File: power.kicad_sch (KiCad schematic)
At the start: 8 parts, among them U8 LM2940S-5.0/NOPB

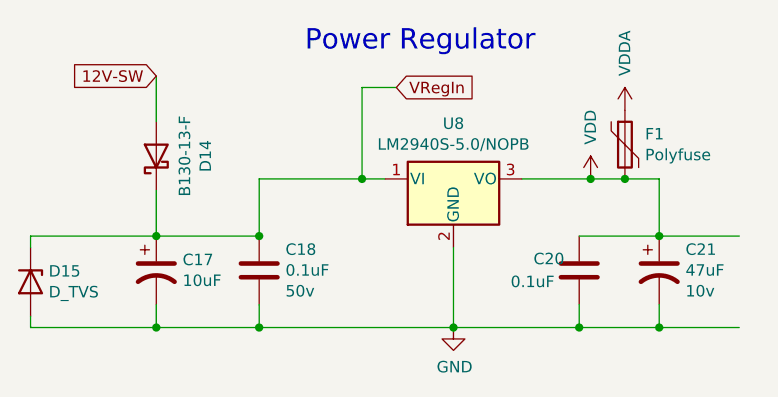
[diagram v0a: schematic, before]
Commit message: Boards should be placed correctly now
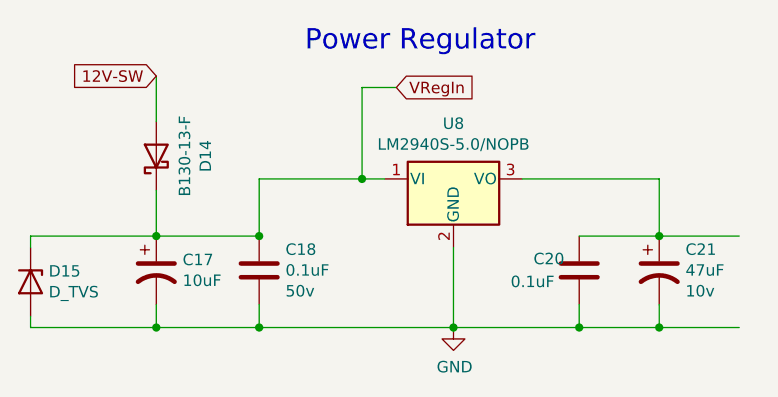
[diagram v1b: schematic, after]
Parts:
- removed F1: Polyfuse, Fuse:Fuse_1812_4532Metric, symbol Device:Polyfuse
- C17: JLCPCB (none) -> C122299
- C18, C20: JLCPCB (none) -> C49678
- C21: JLCPCB (none) -> C7207
- D14: JLCPCB (none) -> C134423
- D15: JLCPCB (none) -> C294881
- U8: footprint Package_TO_SOT_SMD:TO-263-3_TabPin2 -> Package_TO_SOT_SMD:SOT-223; JLCPCB (none) -> C596334
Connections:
- net VDD: no longer names the net of C20.1, C21.1, U8.3 (VO)
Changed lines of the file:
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@@
     (company "Speeduino")
   )
-  (junction (at 176.53 62.23) (diameter 0) (color 0 0 0 0)
-  )
   (junction (at 128.27 78.74) (diameter 0) (color 0 0 0 0)
   )
@@
   (junction (at 128.27 68.58) (diameter 0) (color 0 0 0 0)
   )
-  (junction (at 180.34 62.23) (diameter 0) (color 0 0 0 0)
-  )
   (junction (at 139.7 78.74) (diameter 0) (color 0 0 0 0)
   )
@@
     (stroke (width 0) (type default) (color 0 0 0 0))
   )
-  (wire (pts (xy 168.91 62.23) (xy 176.53 62.23))
+  (wire (pts (xy 168.91 62.23) (xy 184.15 62.23))
     (stroke (width 0) (type default) (color 0 0 0 0))
   )
@@
     (stroke (width 0) (type default) (color 0 0 0 0))
   )
-  (wire (pts (xy 180.34 62.23) (xy 184.15 62.23))
-    (stroke (width 0) (type default) (color 0 0 0 0))
-  )
   (wire (pts (xy 114.3 78.74) (xy 128.27 78.74))
     (stroke (width 0) (type default) (color 0 0 0 0))
   )
   (wire (pts (xy 175.26 76.2) (xy 175.26 78.74))
-    (stroke (width 0) (type default) (color 0 0 0 0))
-  )
-  (wire (pts (xy 176.53 62.23) (xy 180.34 62.23))
     (stroke (width 0) (type default) (color 0 0 0 0))
   )
@@
       (effects (font (size 1.27 1.27)) hide)
     )
+    (property "JLCPCB" "C49678" (id 9) (at 139.7 72.39 0)
+      (effects (font (size 1.27 1.27)) hide)
+    )
     (pin "1")
     (pin "2")
@@
     )
     (property "URL" "https://www.digikey.com/product-detail/en/kemet/T491D106K050AT/399-8361-1-ND/3472084" (id 8) (at 0 144.78 0)
+      (effects (font (size 1.27 1.27)) hide)
+    )
+    (property "JLCPCB" "C122299" (id 9) (at 128.27 72.39 0)
       (effects (font (size 1.27 1.27)) hide)
     )
@@
       (effects (font (size 1.27 1.27)) hide)
     )
-    (pin "1")
-    (pin "2")
-  )
-  (symbol (lib_id "power:VDD") (at 176.53 62.23 0) (unit 1)
-    (in_bom yes) (on_board yes)
-    (property "Reference" "#PWR047" (id 0) (at 176.53 66.04 0)
-      (effects (font (size 1.27 1.27)) hide)
-    )
-    (property "Value" "VDD" (id 1) (at 176.53 58.42 90)
-      (effects (font (size 1.27 1.27)) (justify left))
-    )
-    (property "Footprint" "" (id 2) (at 176.53 62.23 0)
-      (effects (font (size 1.27 1.27)) hide)
-    )
-    (property "Datasheet" "" (id 3) (at 176.53 62.23 0)
-      (effects (font (size 1.27 1.27)) hide)
-    )
-    (pin "1")
+    (property "JLCPCB" "C134423" (id 8) (at 128.27 59.69 0)
+      (effects (font (size 1.27 1.27)) hide)
+    )
+    (pin "1")
+    (pin "2")
   )
   (symbol (lib_id "Device:C") (at 175.26 72.39 0) (unit 1)
@@
       (effects (font (size 1.27 1.27)) hide)
     )
+    (property "JLCPCB" "C49678" (id 8) (at 175.26 72.39 0)
+      (effects (font (size 1.27 1.27)) hide)
+    )
     (pin "1")
     (pin "2")
@@
     )
     (property "URL" "https://www.digikey.com/product-detail/en/avx-corporation/TAJB476K006RNJ/478-1692-1-ND/564724" (id 8) (at 0 144.78 0)
+      (effects (font (size 1.27 1.27)) hide)
+    )
+    (property "JLCPCB" "C7207" (id 9) (at 184.15 72.39 0)
       (effects (font (size 1.27 1.27)) hide)
     )
@@
     (property "Reference" "U8" (id 0) (at 161.29 56.0832 0))
     (property "Value" "LM2940S-5.0/NOPB" (id 1) (at 161.29 58.3946 0))
-    (property "Footprint" "Package_TO_SOT_SMD:TO-263-3_TabPin2" (id 2) (at 161.29 56.515 0)
+    (property "Footprint" "Package_TO_SOT_SMD:SOT-223" (id 2) (at 161.29 56.515 0)
       (effects (font (size 1.27 1.27) italic) hide)
     )
@@
       (effects (font (size 1.27 1.27)) hide)
     )
+    (property "JLCPCB" "C596334" (id 10) (at 161.29 62.23 0)
+      (effects (font (size 1.27 1.27)) hide)
+    )
     (pin "1")
     (pin "2")
     (pin "3")
   )
-  (symbol (lib_id "power:VDDA") (at 180.34 54.61 0) (unit 1)
-    (in_bom yes) (on_board yes)
-    (property "Reference" "#PWR0108" (id 0) (at 180.34 58.42 0)
-      (effects (font (size 1.27 1.27)) hide)
-    )
-    (property "Value" "VDDA" (id 1) (at 180.34 50.8 90)
-      (effects (font (size 1.27 1.27)) (justify left))
-    )
-    (property "Footprint" "" (id 2) (at 180.34 54.61 0)
-      (effects (font (size 1.27 1.27)) hide)
-    )
-    (property "Datasheet" "" (id 3) (at 180.34 54.61 0)
-      (effects (font (size 1.27 1.27)) hide)
-    )
-    (pin "1")
-  )
-  (symbol (lib_id "Device:Polyfuse") (at 180.34 58.42 0) (unit 1)
-    (in_bom yes) (on_board yes)
-    (property "Reference" "F1" (id 0) (at 182.5752 57.2516 0)
-      (effects (font (size 1.27 1.27)) (justify left))
-    )
-    (property "Value" "Polyfuse" (id 1) (at 182.5752 59.563 0)
-      (effects (font (size 1.27 1.27)) (justify left))
-    )
-    (property "Footprint" "Fuse:Fuse_1812_4532Metric" (id 2) (at 181.61 63.5 0)
-      (effects (font (size 1.27 1.27)) (justify left) hide)
-    )
-    (property "Datasheet" "~" (id 3) (at 180.34 58.42 0)
-      (effects (font (size 1.27 1.27)) hide)
-    )
-    (property "Digikey Part Number" "507-1361-1-ND" (id 4) (at 0 116.84 0)
-      (effects (font (size 1.27 1.27)) hide)
-    )
-    (property "Manufacturer_Name" "Bel Fuse" (id 5) (at 0 116.84 0)
-      (effects (font (size 1.27 1.27)) hide)
-    )
-    (property "Manufacturer_Part_Number" "0ZCC0050FF2C" (id 6) (at 0 116.84 0)
-      (effects (font (size 1.27 1.27)) hide)
-    )
-    (property "URL" "https://www.digikey.com.au/product-detail/en/bel-fuse-inc/0ZCC0050FF2C/507-1361-1-ND/1560228" (id 7) (at 0 116.84 0)
-      (effects (font (size 1.27 1.27)) hide)
-    )
-    (pin "1")
-    (pin "2")
-  )
   (symbol (lib_id "Device:D_Zener") (at 114.3 73.66 270) (unit 1)
     (in_bom yes) (on_board yes)
@@
       (effects (font (size 1.27 1.27)) hide)
     )
+    (property "JLCPCB" "C294881" (id 7) (at 114.3 73.66 90)
+      (effects (font (size 1.27 1.27)) hide)
+    )

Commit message: More changes
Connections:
- net +5V: now reaches C20.1, C21.1, U8.3 (VO)
- net 12V-SW renamed +30
- net VRegIn: no longer names the net of C17.1, C18.1, D14.1 (K), D15.1 (K), U8.1 (VI)
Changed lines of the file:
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@@
   (junction (at 184.15 68.58) (diameter 0) (color 0 0 0 0)
   )
-  (junction (at 184.15 78.74) (diameter 0) (color 0 0 0 0)
-  )
-  (junction (at 151.13 62.23) (diameter 0) (color 0 0 0 0)
-  )
   (junction (at 161.29 78.74) (diameter 0) (color 0 0 0 0)
   )
@@
     (stroke (width 0) (type default) (color 0 0 0 0))
   )
-  (wire (pts (xy 154.94 52.07) (xy 151.13 52.07))
-    (stroke (width 0) (type default) (color 0 0 0 0))
-  )
   (wire (pts (xy 114.3 78.74) (xy 114.3 77.47))
     (stroke (width 0) (type default) (color 0 0 0 0))
@@
     (stroke (width 0) (type default) (color 0 0 0 0))
   )
-  (wire (pts (xy 151.13 52.07) (xy 151.13 62.23))
-    (stroke (width 0) (type default) (color 0 0 0 0))
-  )
   (wire (pts (xy 139.7 78.74) (xy 161.29 78.74))
     (stroke (width 0) (type default) (color 0 0 0 0))
@@
     (stroke (width 0) (type default) (color 0 0 0 0))
   )
-  (wire (pts (xy 193.04 78.74) (xy 184.15 78.74))
-    (stroke (width 0) (type default) (color 0 0 0 0))
-  )
   (wire (pts (xy 193.04 68.58) (xy 184.15 68.58))
     (stroke (width 0) (type default) (color 0 0 0 0))
@@
     (stroke (width 0) (type default) (color 0 0 0 0))
   )
-  (wire (pts (xy 139.7 62.23) (xy 151.13 62.23))
-    (stroke (width 0) (type default) (color 0 0 0 0))
-  )
-  (wire (pts (xy 153.67 62.23) (xy 151.13 62.23))
+  (wire (pts (xy 139.7 62.23) (xy 153.67 62.23))
     (stroke (width 0) (type default) (color 0 0 0 0))
   )
@@
     (effects (font (size 2.2606 2.2606)) (justify left bottom))
   )
-  (global_label "VRegIn" (shape input) (at 154.94 52.07 0) (fields_autoplaced)
-    (effects (font (size 1.27 1.27)) (justify left))
-    (property "Intersheet References" "${INTERSHEET_REFS}" (id 0) (at 0 0 0)
-      (effects (font (size 1.27 1.27)) hide)
-    )
-  )
-  (global_label "12V-SW" (shape input) (at 128.27 50.8 180) (fields_autoplaced)
+  (global_label "+30" (shape input) (at 128.27 50.8 180) (fields_autoplaced)
     (effects (font (size 1.27 1.27)) (justify right))
-    (property "Intersheet References" "${INTERSHEET_REFS}" (id 0) (at 0 0 0)
-      (effects (font (size 1.27 1.27)) hide)
+    (property "Intersheet References" "${INTERSHEET_REFS}" (id 0) (at 121.9544 50.7206 0)
+      (effects (font (size 1.27 1.27)) (justify right) hide)
     )
   )
@@
     (pin "2")
   )
+  (symbol (lib_id "power:+5V") (at 193.04 68.58 0) (unit 1)
+    (in_bom yes) (on_board yes) (fields_autoplaced)
+    (property "Reference" "#PWR0154" (id 0) (at 193.04 72.39 0)
+      (effects (font (size 1.27 1.27)) hide)
+    )
+    (property "Value" "+5V" (id 1) (at 193.04 63.5 0))
+    (property "Footprint" "" (id 2) (at 193.04 68.58 0)
+      (effects (font (size 1.27 1.27)) hide)
+    )
+    (property "Datasheet" "" (id 3) (at 193.04 68.58 0)
+      (effects (font (size 1.27 1.27)) hide)
+    )
+    (pin "1")
+  )
 )
